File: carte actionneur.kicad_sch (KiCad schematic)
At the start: 47 parts, among them J1 Conn_01x03_Pin, J10 Conn_01x03_Pin, J11 Conn_01x02, J12 Screw_Terminal_01x02, J13 Screw_Terminal_01x02, J14 Screw_Terminal_01x02, J15 Conn_01x02, J2 Conn_01x02, J3 Conn_01x03_Pin, J4 Conn_01x03_Pin, J4 Connecteur Programmation, J6 Conn_01x03_Pin, J7 Conn_01x03_Pin, J8 Conn_01x03_Pin, J9 Conn_01x03_Pin, Q1 BSS83P, Q2 2N7000, U1 MEGA_PRO_EMBED_CH340G___ATMEG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, U2 LM317_TO-252, U3 ZXBM5210-SP, U4 YAAJ_DCDC_StepDown_LM2596, U5 YAAJ_DCDC_StepDown_LM2596, U6 YAAJ_DCDC_StepDown_LM2596, U7 ZXBM5210-SP

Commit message: test git
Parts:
- removed J1, J3, J4, J6: Conn_01x03_Pin, Connector_PinHeader_2.54mm:PinHeader_1x03_P2.54mm_Vertical, symbol Connector:Conn_01x03_Pin
- added A2, A3: Pololu_Breakout_A4988, Module:Pololu_Breakout-16_15.2x20.3mm, symbol Driver_Motor:Pololu_Breakout_A4988
- added C7, C8, C9: 100µ, symbol Device:C_Polarized
- added J1: Conn_01x02_Pin, Connector_PinHeader_2.54mm:PinHeader_1x03_P2.54mm_Vertical, symbol Connector:Conn_01x02_Pin
- added J16, J18, J20: Screw_Terminal_01x02, TerminalBlockBend:CUI_TBP01R1-508-02BE, symbol Connector:Screw_Terminal_01x02
- added J17, J19, J3: Conn_01x04_Pin, Connector_JST:JST_XH_B4B-XH-A_1x04_P2.50mm_Vertical, symbol Connector:Conn_01x04_Pin
- added JP1: Jumper_2_Open, Jumper:SolderJumper-2_P1.3mm_Open_TrianglePad1.0x1.5mm, symbol Jumper:Jumper_2_Open
- added R8: 100k, Resistor_SMD:R_0805_2012Metric, symbol Device:R
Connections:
- net +5V: now also A1.2 (VDD), A2.2 (VDD), A3.2 (VDD)
- net 12V PWR: now also J1.2 (Pin_2)
- net GND: now also A1.1 (GND), Q2.1 (S), A2.1 (GND), A3.1 (GND), R8.2
- net Reset: now reaches A1.13 (~{RESET})
- net Reset: now also U1.D20, A2.13 (~{RESET}), A3.13 (~{RESET})
- net Sleep: now reaches A1.14 (~{SLEEP})
- net Sleep: now also A2.14 (~{SLEEP}), A3.14 (~{SLEEP})
- net STEP1: now reaches A1.15 (STEP)
- net STEP1: now also U1.D45
- net DIR1: now reaches A1.16 (DIR)
- net DIR1: now also U1.D44
- net at A1.3 (1B): now also J19.4 (Pin_4)
- net at A1.4 (1A): now also J19.3 (Pin_3)
- net at A1.5 (2A): now also J19.2 (Pin_2)
- net at A1.6 (2B): now also J19.1 (Pin_1)
- net at A1.7 (GND): now also C7.2, J16.2 (Pin_2)
- net at A1.8 (VMOT): now also C7.1, J16.1 (Pin_1)
- net Enable: now reaches A1.9 (~{ENABLE})
- net Enable: now also A2.9 (~{ENABLE}), A3.9 (~{ENABLE})
- net DIR3: now reaches U1.D3
- net DIR3: now also A3.16 (DIR)
- net at U1.D46: now also Q2.2 (G), R8.1
- net STEP3: now reaches U1.D5
- net STEP3: now also A3.15 (STEP)
- net DIR2: now reaches U1.D7
- net DIR2: now also A2.16 (DIR)
- net STEP2: now reaches U1.D9
- net STEP2: now also A2.15 (STEP)
- net at Q2.3 (D): now also J1.1 (Pin_1)
- new net: A2.6 (2B), J17.1 (Pin_1)
- new net: A2.5 (2A), J17.2 (Pin_2)
- new net: A2.4 (1A), J17.3 (Pin_3)
- new net: A2.3 (1B), J17.4 (Pin_4)
- new net: A2.8 (VMOT), C8.1, J18.1 (Pin_1)
- new net: A2.7 (GND), C8.2, J18.2 (Pin_2)
- new net: A3.8 (VMOT), C9.1, J20.1 (Pin_1)
- new net: A3.7 (GND), C9.2, J20.2 (Pin_2)
- new net: A3.3 (1B), J3.4 (Pin_4)
- new net: A3.4 (1A), J3.3 (Pin_3)
- new net: A3.5 (2A), J3.2 (Pin_2)
- new net: A3.6 (2B), J3.1 (Pin_1)
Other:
- moved on the sheet: A1, Q2

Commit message: test
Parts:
- added D2: D, Diode_SMD:D_SOD-123, symbol Device:D
- added J21, J6: Conn_01x08_Pin, Connector_PinHeader_2.54mm:PinHeader_1x08_P2.54mm_Vertical, symbol Connector:Conn_01x08_Pin
- added J4: Conn_01x03_Pin, Connector_PinHeader_2.54mm:PinHeader_1x03_P2.54mm_Vertical, symbol Connector:Conn_01x03_Pin
- added JP2, JP3: Jumper_2_Open, Jumper:SolderJumper-2_P1.3mm_Open_TrianglePad1.0x1.5mm, symbol Jumper:Jumper_2_Open
- added R9: 1.2k, Resistor_SMD:R_0805_2012Metric, symbol Device:R
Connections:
- net 12V PWR: now also R9.1; no longer J1.2 (Pin_2)
- net 5V: now also J4.2 (Pin_2)
- net Enable: now also U1.D24
- net GND: now also J4.3 (Pin_3)
- net Sleep: now also U1.D22
- net at A1.10 (MS1): now also A1.11 (MS2), A1.12 (MS3), JP3.2 (B)
- net at U1.A0: now also J21.8 (Pin_8)
- net at U1.A1: now also J6.1 (Pin_1)
- net at U1.A10: now also J21.3 (Pin_3)
- net at U1.A11: now also J6.6 (Pin_6)
- net at U1.A12: now also J21.2 (Pin_2)
- net at U1.A13: now also J6.7 (Pin_7)
- net at U1.A14: now also J21.1 (Pin_1)
- net at U1.A15: now also J6.8 (Pin_8)
- net at U1.A2: now also J21.7 (Pin_7)
- net at U1.A3: now also J6.2 (Pin_2)
- net at U1.A4: now also J21.6 (Pin_6)
- net at U1.A5: now also J6.3 (Pin_3)
- net at U1.A6: now also J21.5 (Pin_5)
- net at U1.A7: now also J6.4 (Pin_4)
- net at U1.A8: now also J21.4 (Pin_4)
- net at U1.A9: now also J6.5 (Pin_5)
- net MS3: now reaches U1.D17
- net MS3: now also JP2.1 (A)
- net MS2: now reaches U1.D19
- net MS2: now also JP1.1 (A)
- net MS1: now reaches U1.D21
- net MS1: now also JP3.1 (A)
- net at Q2.2 (G), R8.1: now also U1.D50; no longer U1.D46
- net at A2.10 (MS1): now also A2.11 (MS2), A2.12 (MS3), JP2.2 (B)
- net at A3.10 (MS1): now also A3.11 (MS2), A3.12 (MS3), JP1.2 (B)
- new net: J4.1 (Pin_1), U1.D46
- new net: D2.1 (K), J1.2 (Pin_2)
- new net: D2.2 (A), R9.2
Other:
- moved on the sheet: JP1

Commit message: shema complet
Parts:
- removed C1: 0.1uF, Capacitor_SMD:C_0805_2012Metric, symbol Device:C
- removed C2: 1uF, Capacitor_SMD:C_0805_2012Metric, symbol Device:C
- removed D2: D, Diode_SMD:D_SOD-123, symbol Device:D
- removed H5, H6, H7, H8: MountingHole_Pad, MountingHole:MountingHole_2.7mm_Pad_Via, symbol Mechanical:MountingHole_Pad
- removed J1: Conn_01x02_Pin, Connector_PinHeader_2.54mm:PinHeader_1x03_P2.54mm_Vertical, symbol Connector:Conn_01x02_Pin
- removed J12, J13, J14, J16, J18, J20: Screw_Terminal_01x02, TerminalBlockBend:CUI_TBP01R1-508-02BE, symbol Connector:Screw_Terminal_01x02
- removed J4: Conn_01x03_Pin, Connector_PinHeader_2.54mm:PinHeader_1x03_P2.54mm_Vertical, symbol Connector:Conn_01x03_Pin
- removed Q1: BSS83P, Package_TO_SOT_SMD:SOT-23, symbol Transistor_FET:BSS83P
- removed Q2: 2N7000, Package_TO_SOT_THT:TO-92_Inline, symbol Transistor_FET:2N7000
- removed R1: 10k, Resistor_SMD:R_0805_2012Metric, symbol Device:R
- removed R2: 4.7k, Resistor_SMD:R_0805_2012Metric, symbol Device:R
- removed R3: 1.5k, Resistor_SMD:R_0805_2012Metric, symbol Device:R
- removed R8: 100k, Resistor_SMD:R_0805_2012Metric, symbol Device:R
- removed U2: LM317_TO-252, Package_TO_SOT_SMD:TO-252-2, symbol Regulator_Linear:LM317_TO-252
- removed U6: YAAJ_DCDC_StepDown_LM2596, lib-buck-converter:YAAJ_DCDC_StepDown_LM2596, symbol yaaj_dcdc_stepdown_lm2596:YAAJ_DCDC_StepDown_LM2596
- added D3, D4, D5: D, Diode_SMD:D_SOD-123, symbol Device:D
- added J1, J25, J26, J27: Conn_01x03_Pin, Connector_PinHeader_2.54mm:PinHeader_1x03_P2.54mm_Vertical, symbol Connector:Conn_01x03_Pin
- added J22, J23, J24: Conn_01x02_Pin, Connector_JST:JST_XH_B2B-XH-A_1x02_P2.50mm_Vertical, symbol Connector:Conn_01x02_Pin
- added JP10, JP11, JP12, JP13, JP14, JP15, JP16, JP17, JP18, JP19, JP20, JP21, JP22, JP23, JP24, JP4, JP5, JP6, JP7, JP8, JP9: Jumper_2_Open, Jumper:SolderJumper-2_P1.3mm_Open_TrianglePad1.0x1.5mm, symbol Jumper:Jumper_2_Open
- added Q1: Q_NMOS_GDS, Package_TO_SOT_SMD:TO-252-2, symbol Device:Q_NMOS_GDS
- added Q2, Q3, Q4: QM6006D, Package_TO_SOT_SMD:TO-252-2, symbol Transistor_FET:QM6006D
- added R10, R11: 100k, Resistor_SMD:R_0805_2012Metric, symbol Device:R
- added R4: 56k, Resistor_SMD:R_0805_2012Metric_Pad1.20x1.40mm_HandSolder, symbol Device:R
- added U2: YAAJ_DCDC_StepDown_LM2596, lib-buck-converter:YAAJ_DCDC_StepDown_LM2596, symbol yaaj_dcdc_stepdown_lm2596:YAAJ_DCDC_StepDown_LM2596
- C7, C8, C9: footprint (none) -> Capacitor_THT:CP_Radial_D8.0mm_P3.50mm
- J2: footprint TerminalBlock:TerminalBlock_bornier-2_P5.08mm -> TerminalBlockBend:CUI_TBP01R1-508-02BE
- R9: value 1.2k -> 100k
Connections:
- net +5V: now also C3.1, C5.1, JP1.1 (A), JP2.1 (A), JP3.1 (A), U3.3 (VDD), U3.6 (VREF), U7.3 (VDD), U7.6 (VREF), JP4.1 (A), JP5.1 (A), JP6.1 (A), JP7.1 (A), JP8.1 (A), JP9.1 (A)
- net DIR1: now also U1.D25; no longer U1.D44
- net DIR2: now also U1.D27; no longer U1.D7
- net DIR3: now also U1.D29; no longer U1.D3
- net FWD1: now also U1.D46; no longer U1.D10
- net FWD2: now also U1.D52; no longer U1.D12
- net GND: now also A1.7 (GND), A2.7 (GND), A3.7 (GND), C7.2, C8.2, C9.2, D1.2 (A), R9.2, J1.3 (Pin_3), J25.3 (Pin_3), J26.3 (Pin_3), J27.3 (Pin_3), Q1.3 (S), Q2.3 (S), Q3.3 (S), Q4.3 (S), R10.2, R11.2, U2.2 (GND), U2.3 (GND); no longer J2.1 (Pin_1)
- net REV1: now also U1.D45; no longer U1.D11
- net REV2: now also U1.D44; no longer U1.D13
- net Reset: now also U1.D23; no longer U1.D20
- net STEP1: now also U1.D3; no longer U1.D45
- net STEP2: now also U1.D2; no longer U1.D9
- net SWCLK: now also U1.D21
- net SWDIO: now also U1.D20
- net at A2.10 (MS1), JP2.2 (B): no longer A2.11 (MS2), A2.12 (MS3)
- net 12V Mot: now reaches A1.8 (VMOT), C7.1
- net 12V Mot: now also A2.8 (VMOT), A3.8 (VMOT), C8.1, C9.1, U1.VIN_1 (VIN), U1.VIN_2 (VIN), U5.4 (Vout), JP12.2 (B), JP15.2 (B), JP18.2 (B), JP21.2 (B), JP24.2 (B)
- net +24V: now reaches U4.1 (Vin)
- net +24V: now also J2.2 (Pin_2), U5.1 (Vin), R4.1, U2.1 (Vin)
- net Servo1: now reaches J7.1 (Pin_1)
- net Servo1: now also U1.D7; no longer U1.D2
- net Enable2: now reaches U1.D26
- net Enable2: now also A3.9 (~{ENABLE})
- net Enable1: now reaches U1.D28
- net Enable1: now also A2.9 (~{ENABLE})
- net Servo2: now reaches J8.1 (Pin_1)
- net Servo2: now also U1.D6; no longer U1.D4
- net ctrlActionneur2: now reaches U1.D42
- net ctrlActionneur2: now also Q3.1 (G), R10.1
- net ctrlActionneur3: now reaches U1.D43
- net ctrlActionneur3: now also Q4.1 (G), R11.1
- net Servo8: now reaches J9.1 (Pin_1)
- net Servo8: now also U1.D12; no longer U1.D6
- net Servo3: now reaches J10.1 (Pin_1)
- net Servo3: now also U1.D9; no longer U1.D8
- removed net +12V: C4.1, C6.1, D1.1 (K), U1.VIN_1 (VIN), U1.VIN_2 (VIN), U3.2 (VM), U7.2 (VM)
- net 12V PWR renamed ctrlActionneur1
- net ctrlActionneur1: now also U1.D4, Q2.1 (G)
- net 5V renamed 5VServo
- net 5VServo: now also J1.2 (Pin_2), J25.2 (Pin_2), J26.2 (Pin_2), J27.2 (Pin_2); no longer U5.4 (Vout)
- net Enable renamed Enable3
- net Enable3: no longer A2.9 (~{ENABLE}), A3.9 (~{ENABLE})
- removed net MS1: JP3.1 (A), U1.D21
- net MS2: no longer names the net of U1.D19
- net MS2: no longer JP1.1 (A)
- net MS3: no longer names the net of U1.D17
- net MS3: no longer JP2.1 (A)
- removed net tension alim moteur DC: C3.1, C5.1, U3.3 (VDD), U3.6 (VREF), U4.4 (Vout), U7.3 (VDD), U7.6 (VREF)
- new net: A1.10 (MS1), JP7.2 (B)
- new net: A1.11 (MS2), JP8.2 (B)
- new net: A1.12 (MS3), JP9.2 (B)
- new net: D4.1 (K), J23.2 (Pin_2), JP13.1 (A), JP14.1 (A), JP15.1 (A)
- new net: D3.1 (K), J22.2 (Pin_2), JP16.1 (A), JP17.1 (A), JP18.1 (A)
- new net: D3.2 (A), J22.1 (Pin_1), Q2.2 (D)
- new net: D5.1 (K), J24.2 (Pin_2), JP10.1 (A), JP11.1 (A), JP12.1 (A)
- new net: A2.11 (MS2), JP1.2 (B)
- new net: C4.1, JP19.1 (A), JP20.1 (A), JP21.1 (A), U3.2 (VM)
- new net: D5.2 (A), J24.1 (Pin_1), Q4.2 (D)
- new net: C6.1, JP22.1 (A), JP23.1 (A), JP24.1 (A), U7.2 (VM)
- new net: A2.12 (MS3), JP3.2 (B)
- new net: D4.2 (A), J23.1 (Pin_1), Q3.2 (D)
- new net: D1.1 (K), Q1.1 (G), R4.2
- new net: A3.10 (MS1), JP4.2 (B)
- new net: A3.11 (MS2), JP5.2 (B)
- new net: A3.12 (MS3), JP6.2 (B)
- new net: J2.1 (Pin_1), Q1.2 (D)
- new net 5V Servo: JP11.2 (B), JP14.2 (B), JP17.2 (B), JP20.2 (B), JP23.2 (B), U2.4 (Vout)
- new net Servo4: J1.1 (Pin_1), U1.D8
- new net Servo5: J25.1 (Pin_1), U1.D11
- new net Servo6: J26.1 (Pin_1), U1.D10
- new net Servo7: J27.1 (Pin_1), U1.D13
- new net VmotDC: JP10.2 (B), JP13.2 (B), JP16.2 (B), JP19.2 (B), JP22.2 (B), U4.4 (Vout)
- no-connect marks 0 -> 31
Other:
- moved on the sheet: A1, A2, A3, C3, C4, C5, C6, C7, H1, H2, H3, J10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

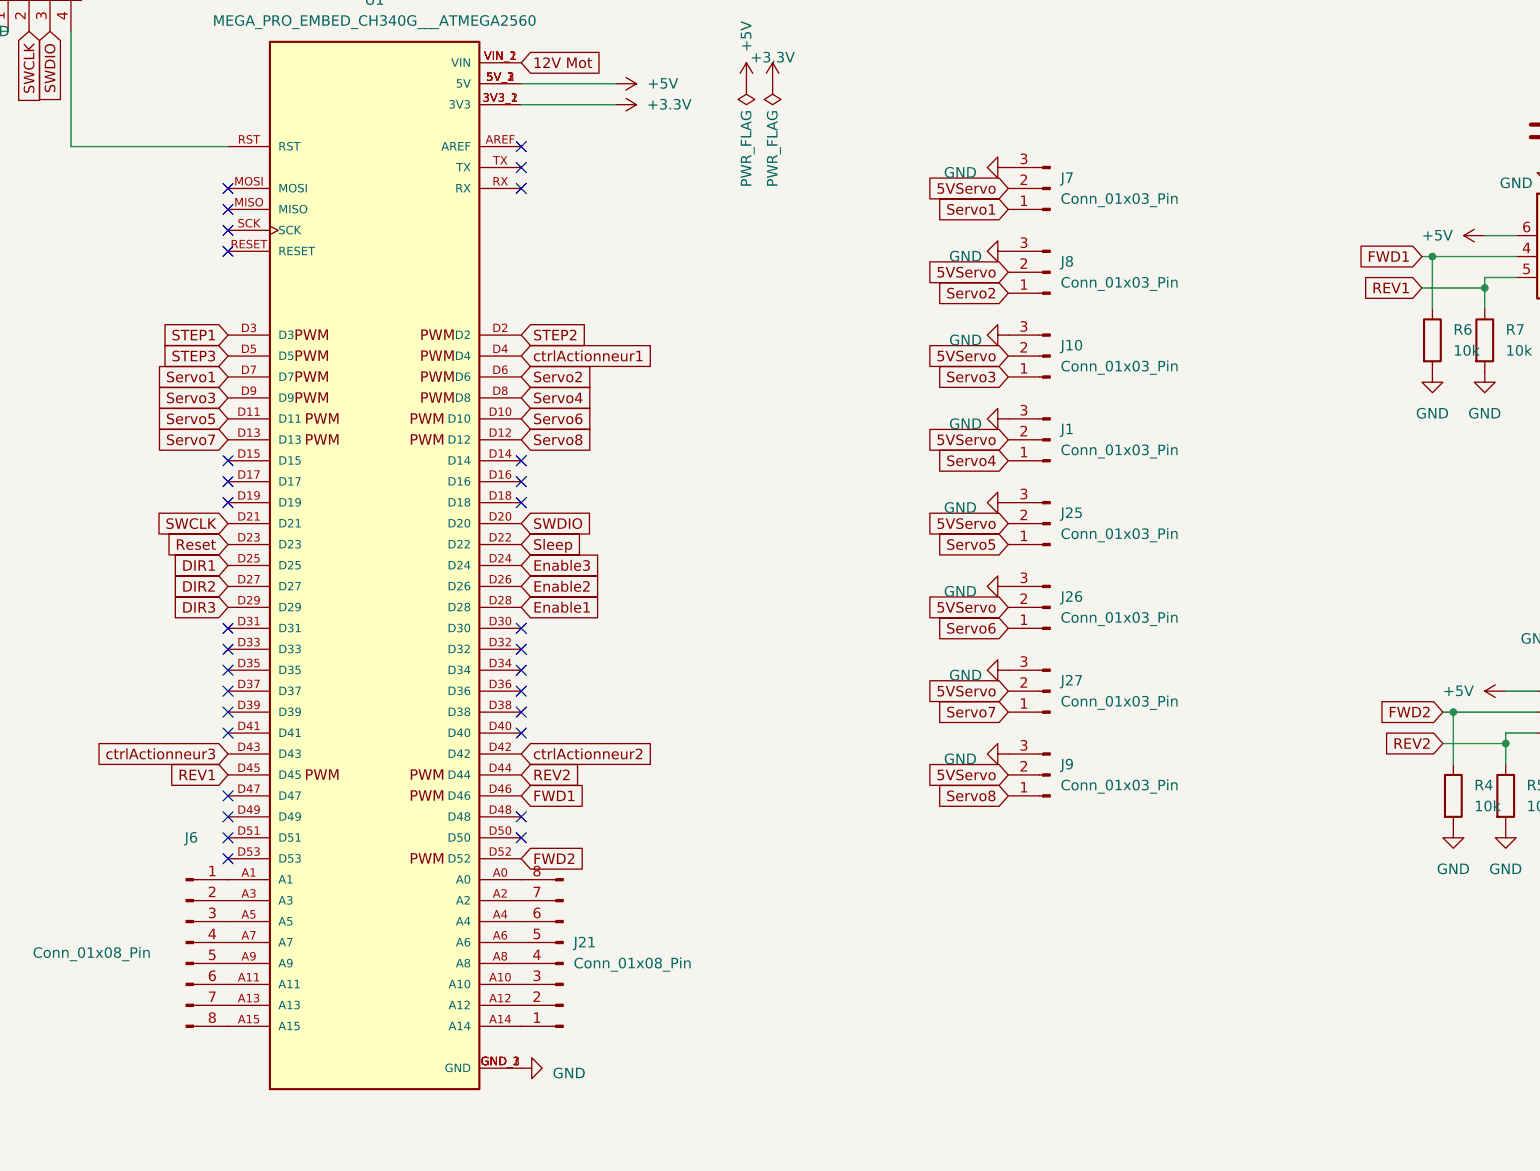
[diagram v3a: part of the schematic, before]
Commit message: ajout prise capteur
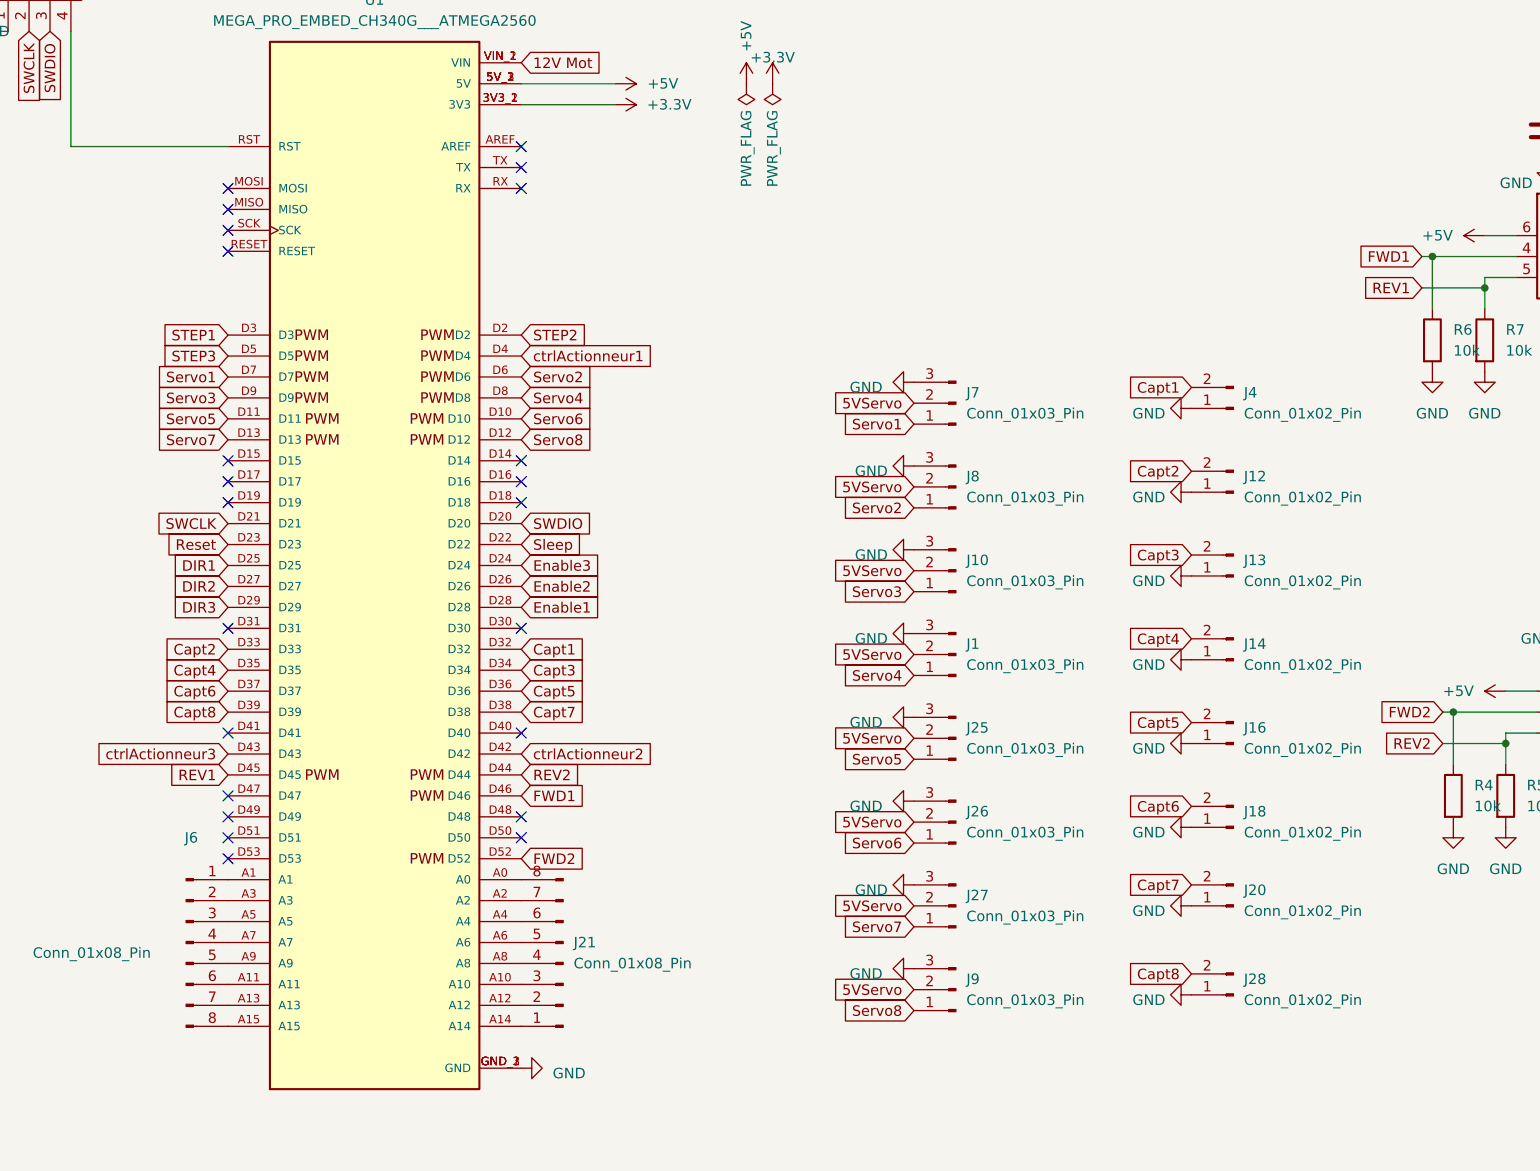
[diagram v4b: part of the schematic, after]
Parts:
- added J12, J13, J14, J16, J18, J20, J28, J4: Conn_01x02_Pin, Connector_PinHeader_2.54mm:PinHeader_1x02_P2.54mm_Vertical, symbol Connector:Conn_01x02_Pin
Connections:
- net GND: now also J12.1 (Pin_1), J13.1 (Pin_1), J14.1 (Pin_1), J16.1 (Pin_1), J18.1 (Pin_1), J20.1 (Pin_1), J28.1 (Pin_1), J4.1 (Pin_1)
- net Capt1: now reaches U1.D32
- net Capt1: now also J4.2 (Pin_2)
- net Capt2: now reaches U1.D33
- net Capt2: now also J12.2 (Pin_2)
- net Capt3: now reaches U1.D34
- net Capt3: now also J13.2 (Pin_2)
- net Capt4: now reaches U1.D35
- net Capt4: now also J14.2 (Pin_2)
- net Capt5: now reaches U1.D36
- net Capt5: now also J16.2 (Pin_2)
- net Capt6: now reaches U1.D37
- net Capt6: now also J18.2 (Pin_2)
- net Capt7: now reaches U1.D38
- net Capt7: now also J20.2 (Pin_2)
- net Capt8: now reaches U1.D39
- net Capt8: now also J28.2 (Pin_2)
- no-connect marks 31 -> 23
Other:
- moved on the sheet: J1, J10, J25, J26, J27, J7, J8, J9

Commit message: modification 3
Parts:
- A1, A2, A3: footprint Module:Pololu_Breakout-16_15.2x20.3mm -> A4988:Pololu_Breakout-16_15.2x20.3mm
- U1: footprint lib:MODULE_MEGA_PRO_EMBED_CH340G___ATMEGA2560 -> lib-arduino:MODULE_MEGA_PRO_EMBED_CH340G___ATMEGA2560
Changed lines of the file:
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@@
       (effects (font (size 1.27 1.27)) (justify left))
     )
-    (property "Footprint" "Module:Pololu_Breakout-16_15.2x20.3mm" (at 77.47 170.18 0)
+    (property "Footprint" "A4988:Pololu_Breakout-16_15.2x20.3mm" (at 77.47 170.18 0)
       (effects (font (size 1.27 1.27)) (justify left) hide)
     )
@@
       (effects (font (size 1.27 1.27)))
     )
-    (property "Footprint" "lib:MODULE_MEGA_PRO_EMBED_CH340G___ATMEGA2560" (at 219.075 93.345 0)
+    (property "Footprint" "lib-arduino:MODULE_MEGA_PRO_EMBED_CH340G___ATMEGA2560" (at 219.075 93.345 0)
       (effects (font (size 1.27 1.27)) (justify bottom) hide)
     )
@@
       (effects (font (size 1.27 1.27)) (justify left))
     )
-    (property "Footprint" "Module:Pololu_Breakout-16_15.2x20.3mm" (at 76.835 64.77 0)
+    (property "Footprint" "A4988:Pololu_Breakout-16_15.2x20.3mm" (at 76.835 64.77 0)
       (effects (font (size 1.27 1.27)) (justify left) hide)
     )
@@
       (effects (font (size 1.27 1.27)) (justify left))
     )
-    (property "Footprint" "Module:Pololu_Breakout-16_15.2x20.3mm" (at 76.835 116.205 0)
+    (property "Footprint" "A4988:Pololu_Breakout-16_15.2x20.3mm" (at 76.835 116.205 0)
       (effects (font (size 1.27 1.27)) (justify left) hide)
     )
